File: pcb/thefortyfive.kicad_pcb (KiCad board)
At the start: 2 copper layers, 256 x 81 mm, 117 parts, among them J1 Conn_01x16_Female, J2 Conn_01x12_Female

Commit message: fix issue with reversed connector
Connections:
- J2 pad 1: Row8 -> Net-(J2-Pad1)
- J2 pad 10: Net-(J2-Pad10) -> Col6
- J2 pad 11: Net-(J2-Pad11) -> Col7
- J2 pad 12: Net-(J2-Pad12) -> Row7
- J2 pad 2: Col1 -> Net-(J2-Pad2)
- J2 pad 3: Col2 -> Net-(J2-Pad3)
- J2 pad 4: Col3 -> Row8
- J2 pad 5: Col4 -> Col1
- J2 pad 6: Col5 -> Col2
- J2 pad 7: Col6 -> Col3
- J2 pad 8: Col7 -> Col4
- J2 pad 9: Row7 -> Col5
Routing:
- net Col3: track 432.0 -> 545.1 mm
- net Row5: track 323.6 -> 299.4 mm
- net Col5: track 377.1 -> 386.3 mm
- net Col6: track 463.7 -> 457.1 mm
- net Col4: track 422.0 -> 428.3 mm
- net Row7: track 263.8 -> 269.9 mm
- net Col7: track 90.6 -> 94.2 mm
- net Col2: track 416.0 -> 417.9 mm
- net Col1: track 317.0 -> 315.1 mm
- net Row8: track 187.8 -> 188.8 mm

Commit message: remove all switch options
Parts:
- removed D4, D44, D49: D_SOD-123, Diode_SMD:D_SOD-123
- removed MX1,1:1, MX2,6:1: MX-NoLED, MX_Alps_Hybrid:MXOnly-1.5U-NoLED
- removed MX3,1:1, MX6,6:1: MX-NoLED, MX_Alps_Hybrid:MXOnly-1.75U-NoLED
- removed MX4,5:1, MX7,2:1, MX7,3:1, MX7,3:2, MX8,4:1, MX8,4:2, MX8,5:1: MX-NoLED, MX_Alps_Hybrid:MXOnly-1U-NoLED
- removed MX4,6:1, MX5,1:1: MX-NoLED, MX_Alps_Hybrid:MXOnly-2.25U-NoLED
- removed MX4,6:2, MX7,3:3, MX7,4:1, MX8,3:1, MX8,4:3, MX8,6:1: MX-NoLED, MX_Alps_Hybrid:MXOnly-1.25U-NoLED
- removed MX7,1:1: MX-NoLE, MX_Alps_Hybrid:MXOnly-1.25U-NoLED
- moved D48 17.8 mm to (272.7, 103.0)
- moved D46 16.7 mm to (275.1, 65.0)
- moved D47 12.3 mm to (268.1, 83.9), turned to 90 degrees
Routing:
- net Col6: track 457.1 -> 421.3 mm
- net Col1: track 315.1 -> 283.8 mm
- net Row7: track 269.9 -> 243.9 mm
- net Row6: track 146.4 -> 171.7 mm
- net Net-(D47-Pad2): track 27.8 -> 6.10 mm
- net Row2: track 138.0 -> 155.6 mm
- net Col3: track 545.1 -> 529.1 mm
- net Net-(D46-Pad2): track 20.5 -> 6.05 mm
- net Col2: track 417.9 -> 406.8 mm
- net Net-(D48-Pad2): track 17.1 -> 6.07 mm
- net Net-(D44-Pad2): track 10.9 -> 0.00 mm
- net Net-(D49-Pad2): track 10.4 -> 0.00 mm
- net Col5: track 386.3 -> 377.5 mm
- net Col7: track 94.2 -> 85.9 mm
- net Net-(D4-Pad2): track 5.85 -> 0.00 mm
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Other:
- board text removed: "1"
- board text removed: "2"
- board text removed: "3"
- board text removed: "MX4,5"
- board text removed: "MX7,1"
- board text removed: "MX8,6"

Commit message: reduce width, update version message
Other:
- board size 256 x 81 mm -> 252.4 x 81 mm
- board text added: "thefortyfive v0.2"
- board text added: "with love from Old Badger"
- board text removed: "thefortyfive v0.1"
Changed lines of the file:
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@@
     )
   )
-  (gr_text "thefortyfive v0.1" (at 260.747094 133.350112) (layer B.Mask)
+  (gr_text "with love from Old Badger" (at 56.35625 133.35) (layer B.Mask)
     (effects (font (size 2.54 2.54) (thickness 0.15) italic) (justify mirror))
   )
-  (gr_text "thefortyfive v0.1" (at 44.053162 133.350112) (layer F.Mask)
-    (effects (font (size 2.54 2.54) (thickness 0.15) italic))
+  (gr_text "thefortyfive v0.2" (at 257.96875 133.35) (layer B.Mask)
+    (effects (font (size 2.54 2.54) (thickness 0.15) italic) (justify mirror))
   )
-  (dimension 255.98459 (width 0.15) (layer Dwgs.User)
-    (gr_text "10.0781 in" (at 152.400128 153.107948) (layer Dwgs.User)
+  (dimension 254.793827 (width 0.15) (layer Dwgs.User)
+    (gr_text "10.0313 in" (at 151.222126 152.807087 0.04459712448) (layer Dwgs.User)
       (effects (font (size 1 1) (thickness 0.15)))
     )
-    (feature1 (pts (xy 280.392423 136.326677) (xy 280.392423 152.394369)))
-    (feature2 (pts (xy 24.407833 136.326677) (xy 24.407833 152.394369)))
-    (crossbar (pts (xy 24.407833 151.807948) (xy 280.392423 151.807948)))
-    (arrow1a (pts (xy 280.392423 151.807948) (xy 279.265919 152.394369)))
-    (arrow1b (pts (xy 280.392423 151.807948) (xy 279.265919 151.221527)))
-    (arrow2a (pts (xy 24.407833 151.807948) (xy 25.534337 152.394369)))
-    (arrow2b (pts (xy 24.407833 151.807948) (xy 25.534337 151.221527)))
+    (feature1 (pts (xy 278.60625 136.326677) (xy 278.618445 151.994347)))
+    (feature2 (pts (xy 23.8125 136.525) (xy 23.824695 152.19267)))
+    (crossbar (pts (xy 23.824239 151.606249) (xy 278.617989 151.407926)))
+    (arrow1a (pts (xy 278.617989 151.407926) (xy 277.491942 151.995223)))
+    (arrow1b (pts (xy 278.617989 151.407926) (xy 277.491029 150.822382)))
+    (arrow2a (pts (xy 23.824239 151.606249) (xy 24.951199 152.191793)))
+    (arrow2b (pts (xy 23.824239 151.606249) (xy 24.950286 151.018952)))
   )
   (dimension 80.962586 (width 0.15) (layer Dwgs.User)
@@
     (arrow2b (pts (xy 14.882825 56.554717) (xy 15.469246 57.681221)))
   )
-  (gr_arc (start 29.170337 132.754799) (end 24.407837 132.754799) (angle -90) (layer Edge.Cuts) (width 0.05))
-  (gr_arc (start 29.170337 61.317239) (end 29.170337 56.554735) (angle -90) (layer Edge.Cuts) (width 0.05))
-  (gr_arc (start 275.629919 61.317217) (end 280.392419 61.317217) (angle -90) (layer Edge.Cuts) (width 0.05))
-  (gr_arc (start 275.629919 132.754717) (end 275.629919 137.517217) (angle -90) (layer Edge.Cuts) (width 0.05))
-  (gr_line (start 29.170337 137.517303) (end 275.629919 137.517217) (layer Edge.Cuts) (width 0.05))
-  (gr_line (start 29.170337 56.554735) (end 275.629919 56.554717) (layer Edge.Cuts) (width 0.05))
-  (gr_line (start 24.407833 61.317239) (end 24.407837 132.754799) (layer Edge.Cuts) (width 0.05))
-  (gr_line (start 280.392419 61.317217) (end 280.392419 132.754777) (layer Edge.Cuts) (width 0.05))
+  (gr_arc (start 30.95625 132.754799) (end 26.19375 132.754799) (angle -90) (layer Edge.Cuts) (width 0.05))
+  (gr_arc (start 30.956254 61.317239) (end 30.956254 56.554735) (angle -90) (layer Edge.Cuts) (width 0.05))
+  (gr_arc (start 273.84375 61.317217) (end 278.60625 61.317217) (angle -90) (layer Edge.Cuts) (width 0.05))
+  (gr_arc (start 273.84375 132.754717) (end 273.84375 137.517217) (angle -90) (layer Edge.Cuts) (width 0.05))
+  (gr_line (start 30.95625 137.517299) (end 273.84375 137.517217) (layer Edge.Cuts) (width 0.05))
+  (gr_line (start 30.95625 56.554735) (end 273.84375 56.554717) (layer Edge.Cuts) (width 0.05))
+  (gr_line (start 26.19375 61.317239) (end 26.193754 132.754799) (layer Edge.Cuts) (width 0.05))
+  (gr_line (start 278.60625 61.317217) (end 278.60625 132.754777) (layer Edge.Cuts) (width 0.05))
   (segment (start 46.292504 63.380967) (end 46.434379 63.239092) (width 0.25) (layer B.Cu) (net 1))
   (segment (start 40.640004 63.380967) (end 46.292504 63.380967) (width 0.25) (layer B.Cu) (net 1))

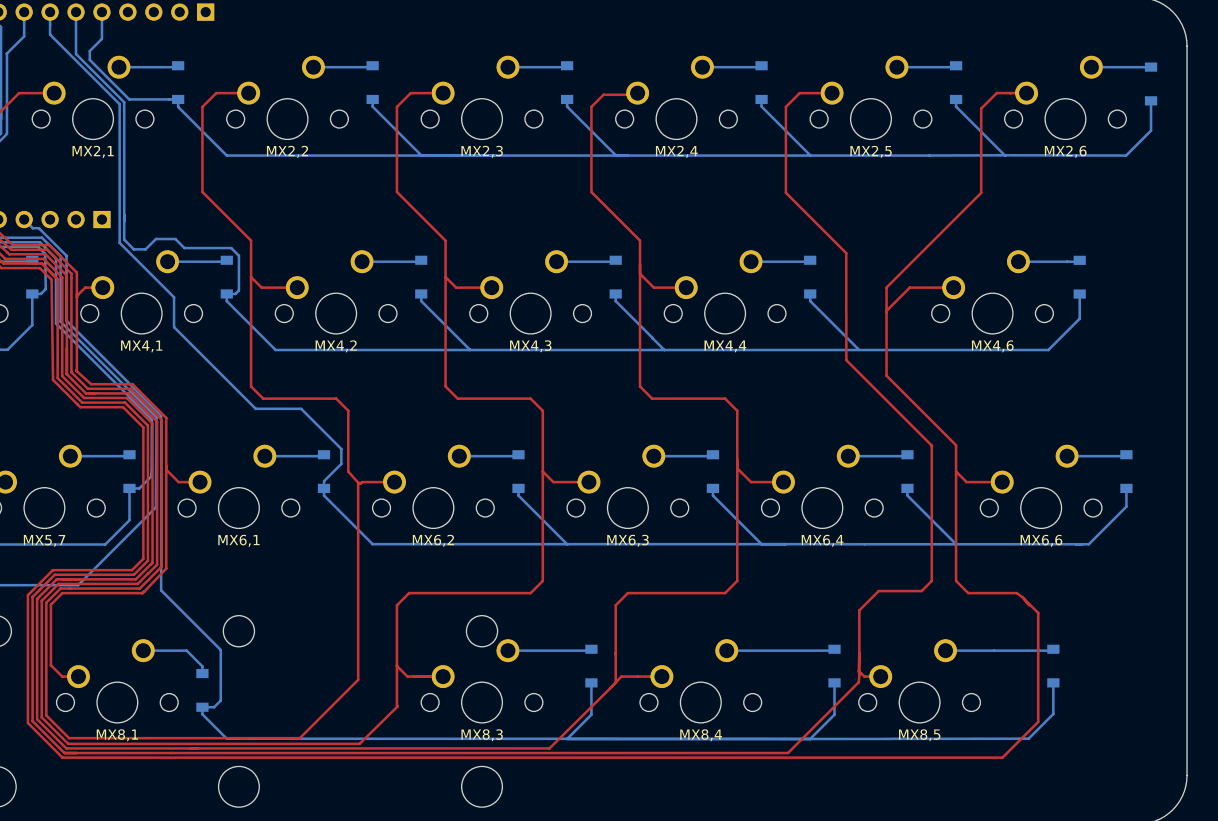
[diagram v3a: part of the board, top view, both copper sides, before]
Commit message: reroute tracks away from edges
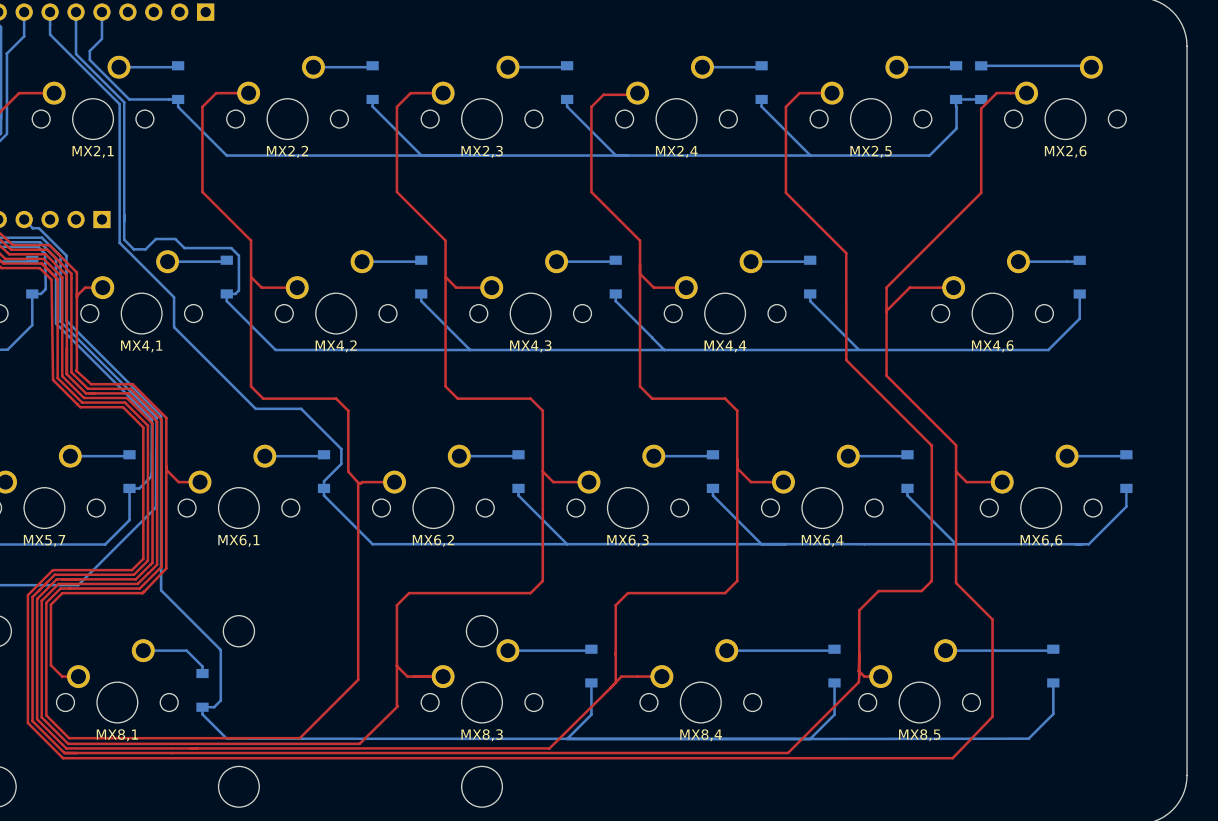
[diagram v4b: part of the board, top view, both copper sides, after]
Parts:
- moved D46 16.6 mm to (258.4, 64.9)
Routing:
- net Row2: track 155.6 -> 131.5 mm
- net Col6: track 421.3 -> 411.0 mm
- net Net-(D46-Pad2): track 6.05 -> 11.1 mm

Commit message: added reset button
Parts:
- added REF**: MountingHole_2.2mm_M2, MountingHole:MountingHole_2.2mm_M2, F.Cu at (123.8, 60.3)
- added REF**: MountingHole_2.2mm_M2, MountingHole:MountingHole_2.2mm_M2, F.Cu at (200.0, 60.3)
- added REF**: MountingHole_2.2mm_M2, MountingHole:MountingHole_2.2mm_M2, F.Cu at (197.6, 133.3)
- added REF**: MountingHole_2.2mm_M2, MountingHole:MountingHole_2.2mm_M2, F.Cu at (107.2, 133.3)
- added REF**: MountingHole_2.2mm_M2, MountingHole:MountingHole_2.2mm_M2, F.Cu at (30.2, 133.3)
- added REF**: MountingHole_2.2mm_M2, MountingHole:MountingHole_2.2mm_M2, F.Cu at (274.6, 133.3)
- added REF**: MountingHole_2.2mm_M2, MountingHole:MountingHole_2.2mm_M2, F.Cu at (274.6, 60.3)
- added REF**: MountingHole_2.2mm_M2, MountingHole:MountingHole_2.2mm_M2, F.Cu at (30.2, 60.3)
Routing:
- net Col4: track 424.2 -> 496.1 mm
- net Col3: track 529.1 -> 459.8 mm
- net Col1: track 283.8 -> 288.2 mm
- net Col5: track 377.5 -> 381.1 mm
- net Col2: track 406.8 -> 409.8 mm

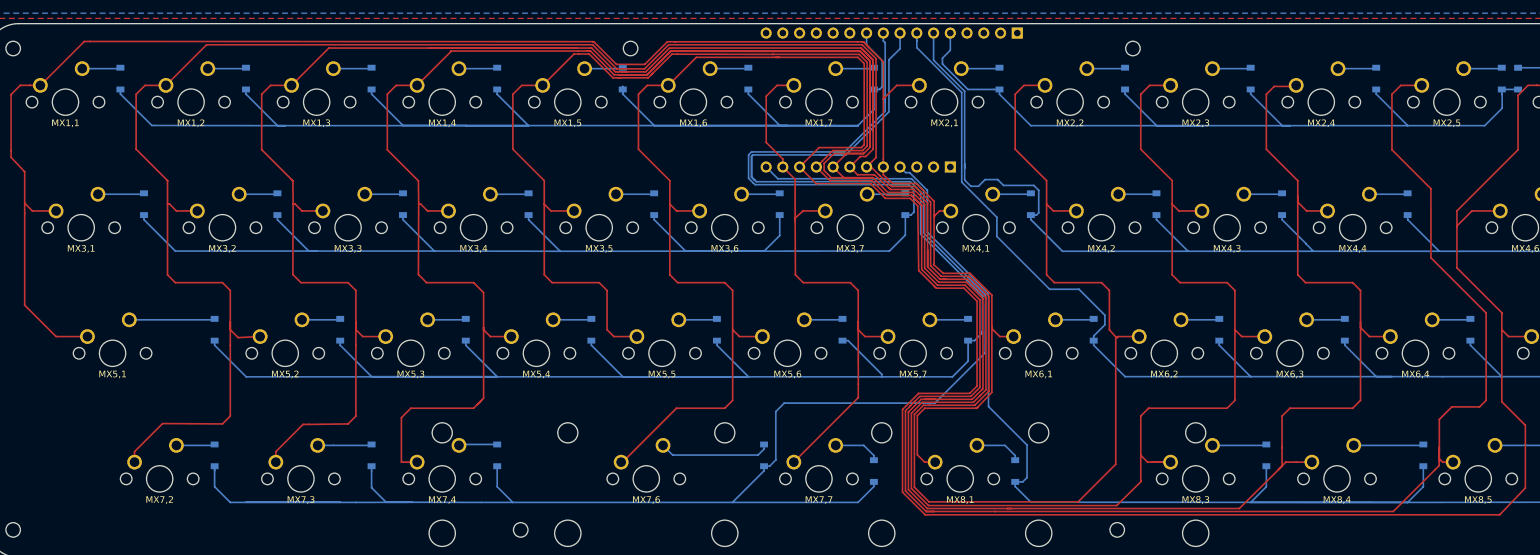
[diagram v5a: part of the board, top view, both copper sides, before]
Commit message: adjust routing around mounting holes
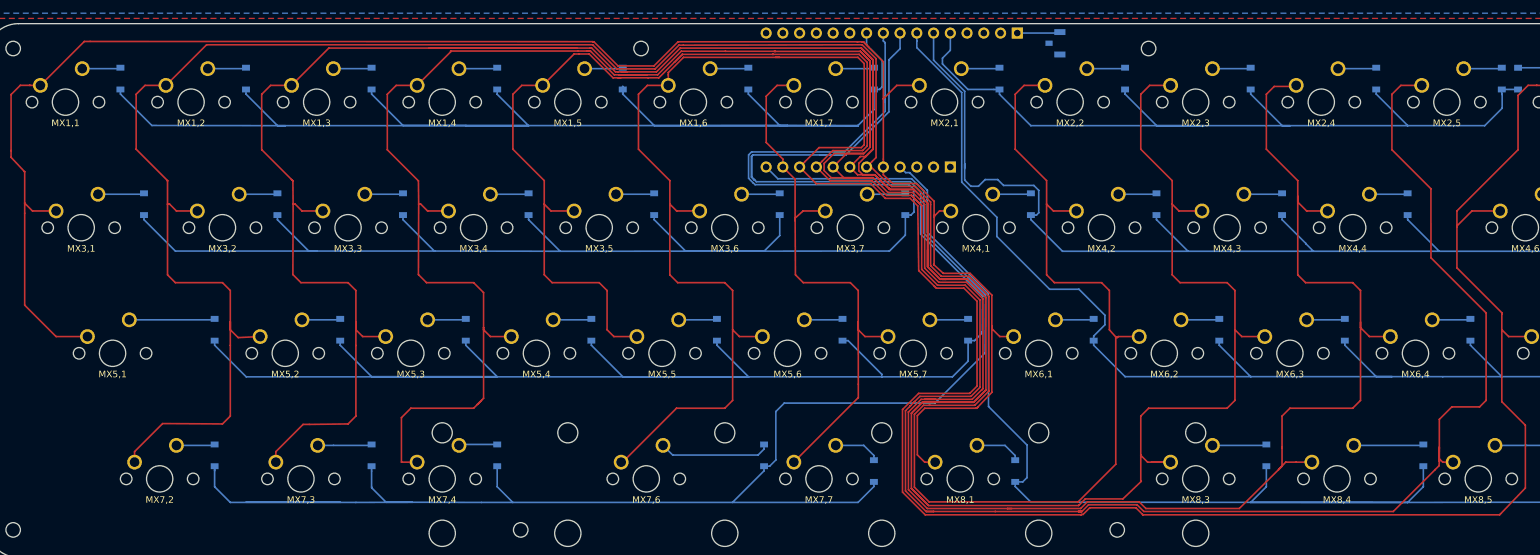
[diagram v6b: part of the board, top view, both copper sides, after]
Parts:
- added SW1: SW_Push, Button_Switch_SMD:SW_SPST_B3U-1100P, B.Cu at (188.1, 59.5)
- moved REF** 2.38 mm to (202.4, 60.3)
- moved REF** 1.59 mm to (125.4, 60.3)
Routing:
- net Col3: track 459.8 -> 525.3 mm
- net Col4: track 496.1 -> 463.3 mm
- net Net-(J1-Pad1): track 0.00 -> 6.52 mm
- net Col5: track 381.1 -> 384.4 mm
- net Col6: track 411.0 -> 413.0 mm

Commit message: reposition mounting holes
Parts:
- moved REF** 1.59 mm to (274.6, 61.9)
- moved REF** 1.59 mm to (30.2, 61.9)
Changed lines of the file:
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@@
   )
   (layers
-    (0 F.Cu signal)
-    (31 B.Cu signal hide)
+    (0 F.Cu signal hide)
+    (31 B.Cu signal)
     (32 B.Adhes user)
     (33 F.Adhes user)
@@
   )
   (module MountingHole:MountingHole_2.2mm_M2 (layer F.Cu)
-    (at 274.6375 60.325)
-    (descr "Mounting Hole 2.2mm, no annular, M2")
-    (tags "mounting hole 2.2mm no annular m2")
-    (attr virtual)
-    (fp_text reference REF** (at 0 -3.2) (layer F.SilkS) hide
-      (effects (font (size 1 1) (thickness 0.15)))
-    )
-    (fp_text value MountingHole_2.2mm_M2 (at 0 3.2) (layer F.Fab)
-      (effects (font (size 1 1) (thickness 0.15)))
-    )
-    (fp_text user %R (at 0.3 0) (layer F.Fab)
-      (effects (font (size 1 1) (thickness 0.15)))
-    )
-    (fp_circle (center 0 0) (end 2.2 0) (layer Cmts.User) (width 0.15))
-    (fp_circle (center 0 0) (end 2.45 0) (layer F.CrtYd) (width 0.05))
-    (pad 1 np_thru_hole circle (at 0 0) (size 2.2 2.2) (drill 2.2) (layers *.Cu *.Mask))
-  )
-  (module MountingHole:MountingHole_2.2mm_M2 (layer F.Cu)
-    (at 30.1625 60.325)
-    (descr "Mounting Hole 2.2mm, no annular, M2")
-    (tags "mounting hole 2.2mm no annular m2")
+    (at 274.6375 61.9125)
+    (descr "Mounting Hole 2.2mm, no annular, M2")
+    (tags "mounting hole 2.2mm no annular m2")
+    (attr virtual)
+    (fp_text reference REF** (at 0 -3.2) (layer F.SilkS) hide
+      (effects (font (size 1 1) (thickness 0.15)))
+    )
+    (fp_text value MountingHole_2.2mm_M2 (at 0 3.2) (layer F.Fab)
+      (effects (font (size 1 1) (thickness 0.15)))
+    )
+    (fp_text user %R (at 0.3 0) (layer F.Fab)
+      (effects (font (size 1 1) (thickness 0.15)))
+    )
+    (fp_circle (center 0 0) (end 2.2 0) (layer Cmts.User) (width 0.15))
+    (fp_circle (center 0 0) (end 2.45 0) (layer F.CrtYd) (width 0.05))
+    (pad 1 np_thru_hole circle (at 0 0) (size 2.2 2.2) (drill 2.2) (layers *.Cu *.Mask))
+  )
+  (module MountingHole:MountingHole_2.2mm_M2 (layer F.Cu)
+    (at 30.1625 61.9125)
+    (descr "Mounting Hole 2.2mm, no annular, M2")
+    (tags "mounting hole 2.2mm no annular m2")
